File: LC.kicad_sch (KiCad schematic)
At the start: 41 parts, among them J4 Conn_01x01_Pin, J5 Conn_01x01_Pin, J6 Conn_01x01_Pin, Q10 NMOS, Q11 NMOS, Q12 NMOS, Q7 NMOS, Q8 NMOS, Q9 NMOS, U3 OPA2196xDGK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

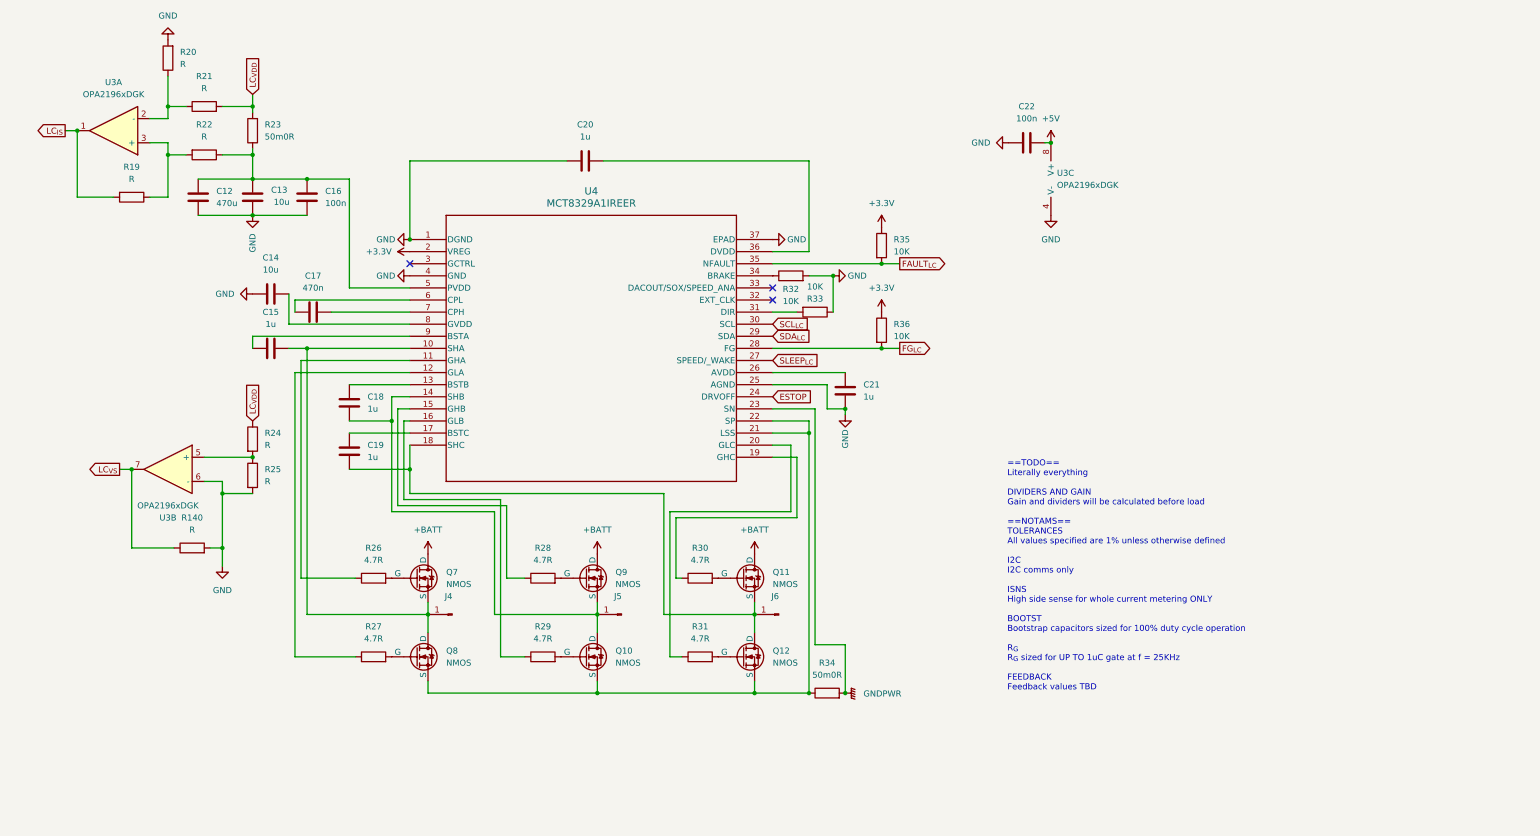
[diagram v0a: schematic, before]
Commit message: The great decluttering
Moved all possible controls to I2C, part selection commenced, IOs assigned pending comms schema
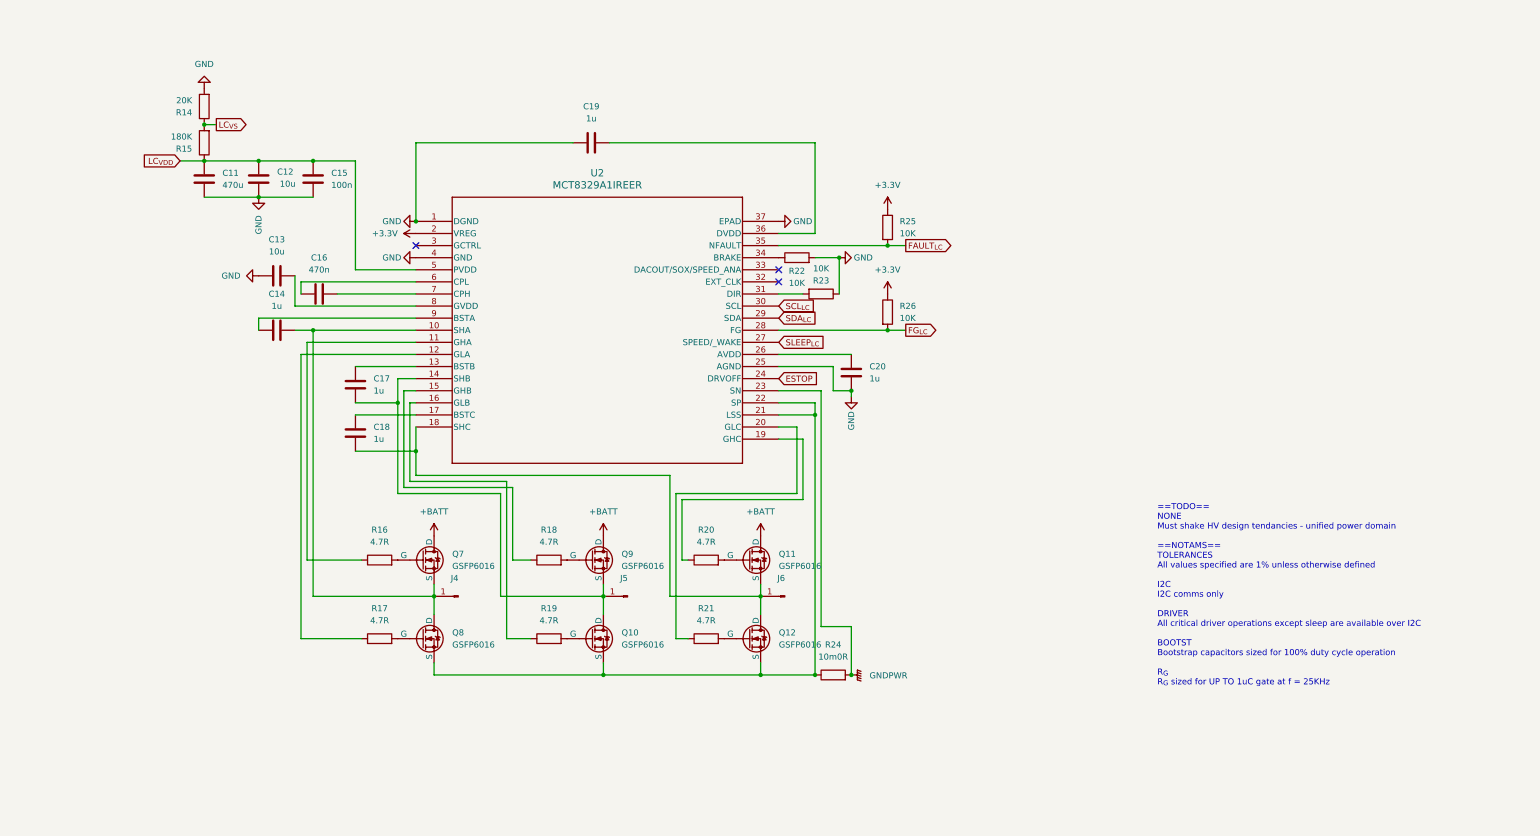
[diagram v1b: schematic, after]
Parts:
- removed C21: 1u, Capacitor_SMD:C_0603_1608Metric, symbol Device:C
- removed C22: 100n, Capacitor_SMD:C_0603_1608Metric, symbol Device:C
- removed R140: R, Resistor_SMD:R_0603_1608Metric_Pad0.98x0.95mm_HandSolder, symbol Device:R
- removed R27, R28, R29, R30, R31: 4.7R, Resistor_SMD:R_1206_3216Metric, symbol Device:R
- removed R32, R33, R35, R36: 10K, Resistor_SMD:R_0603_1608Metric_Pad0.98x0.95mm_HandSolder, symbol Device:R
- removed R34: 50m0R, Resistor_SMD:R_1206_3216Metric, symbol Device:R
- removed U3: OPA2196xDGK, Package_SO:VSSOP-8_3x3mm_P0.65mm, symbol Amplifier_Operational:OPA2196xDGK
- removed U4: MCT8329A1IREER, footprints:WQFN36_REE_TEX, symbol MCT8329:MCT8329A1IREER
- added C11: 470u, Capacitor_SMD:C_0603_1608Metric, symbol Device:C
- added R14: 20K, Resistor_SMD:R_0603_1608Metric_Pad0.98x0.95mm_HandSolder, symbol Device:R
- added R15: 180K, Resistor_SMD:R_0603_1608Metric_Pad0.98x0.95mm_HandSolder, symbol Device:R
- added R16, R17, R18: 4.7R, Resistor_SMD:R_1206_3216Metric, symbol Device:R
- added U2: MCT8329A1IREER, footprints:WQFN36_REE_TEX, symbol MCT8329:MCT8329A1IREER
- C12: value 470u -> 10u
- C14: value 10u -> 1u
- C15: value 1u -> 100n
- C16: value 100n -> 470n
- C17: value 470n -> 1u
- Q10, Q11, Q12, Q7, Q8, Q9: value NMOS -> GSFP6016; footprint (none) -> Package_DFN_QFN:PQFN-8-EP_6x5mm_P1.27mm_Generic
- R19, R20, R21: value R -> 4.7R; footprint Resistor_SMD:R_0603_1608Metric_Pad0.98x0.95mm_HandSolder -> Resistor_SMD:R_1206_3216Metric
- R22, R25: value R -> 10K
- R23: value 50m0R -> 10K; footprint Resistor_SMD:R_1206_3216Metric -> Resistor_SMD:R_0603_1608Metric_Pad0.98x0.95mm_HandSolder
- R24: value R -> 10m0R; footprint Resistor_SMD:R_0603_1608Metric_Pad0.98x0.95mm_HandSolder -> Resistor_SMD:R_1206_3216Metric
- R26: value 4.7R -> 10K; footprint Resistor_SMD:R_1206_3216Metric -> Resistor_SMD:R_0603_1608Metric_Pad0.98x0.95mm_HandSolder
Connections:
- net LC_{IS} is gone; now on an unnamed net: R19.2
- net +3.3V: now also R25.1, R26.1, U2.2 (VREG)
- net ESTOP: now also U2.24 (DRVOFF)
- net FAULT_{LC}: now also R25.2, U2.35 (NFAULT)
- net FG_{LC}: now also R26.2, U2.28 (FG)
- net GND: now also C13.1, C15.2, C19.1, R22.2, R23.1, C11.2, R14.2, U2.1 (DGND), U2.25 (AGND), U2.37 (EPAD), U2.4 (GND); no longer C13.2, C14.1, C16.2, R20.2, R25.2
- net GNDPWR: now also R24.2, U2.23 (SN)
- net LC_{VDD}: now also C12.1, C15.1, C11.1, R15.1, U2.5 (PVDD); no longer R21.2, R23.2, R24.1
- net LC_{VS}: now also R14.1, R15.2
- net SCL_{LC}: now also U2.30 (SCL)
- net SDA_{LC}: now also U2.29 (SDA)
- net SLEEP_{LC}: now also U2.27 (SPEED/_WAKE)
- net at J6.1 (Pin_1), Q11.3 (S), Q12.1 (D): now also C18.2, U2.18 (SHC); no longer C19.2
- net at J5.1 (Pin_1), Q10.1 (D), Q9.3 (S): now also C17.2, U2.14 (SHB); no longer C18.2
- net at Q10.3 (S), Q12.3 (S), Q8.3 (S): now also R24.1, U2.21 (LSS), U2.22 (SP)
- net at R19.1: now also U2.16 (GLB); no longer R22.2
- net at R20.1: now also U2.19 (GHC); no longer R21.1
- net at Q11.2 (G): now also R20.2
- net at Q7.2 (G): now also R16.2; no longer R26.2
- net at J4.1 (Pin_1), Q7.3 (S), Q8.1 (D): now also C14.1, U2.10 (SHA); no longer C15.1
- net at Q9.2 (G): now also R18.2
- net at C18.1: now also U2.17 (BSTC)
- net at C20.2: now also U2.26 (AVDD)
- net at C17.1: now also U2.13 (BSTB)
- net at C14.2: now also U2.9 (BSTA)
- net at Q12.2 (G): now also R21.2
- net at Q8.2 (G): now also R17.2
- new net: C13.2, U2.8 (GVDD)
- new net: R18.1, U2.15 (GHB)
- new net: C19.2, U2.36 (DVDD)
- new net: C16.1, U2.6 (CPL)
- new net: C16.2, U2.7 (CPH)
- new net: R21.1, U2.20 (GLC)
- new net: R23.2, U2.31 (DIR)
- new net: R16.1, U2.11 (GHA)
- new net: R22.1, U2.34 (BRAKE)
- new net: R17.1, U2.12 (GLA)
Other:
- note added: "==TODO== NONE Must shake HV design tendancies - unified power domain ==NOTAMS== TOLERANCES All values specified are 1% unless otherwise defined I2C I2C comms only DRIVER All critical driver operations except sleep are available over I2C BOOTST Bootstrap capacitors sized for 100% duty cycle operation R_{G} R_{G} sized for UP TO 1uC gate at f = 25KHz"
- note removed: "==TODO== Literally everything DIVIDERS AND GAIN Gain and dividers will be calculated before load ==NOTAMS== TOLERANCES All values specified are 1% unless otherwise defined I2C I2C comms only ISNS High side sense for whole current metering ONLY BOOTST Bootstrap capacitors sized for 100% duty cycle operation R_{G} R_{G} sized for UP TO 1uC gate at f = 25KHz FEEDBACK Feedback values TBD"

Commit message: Powerstage
Powerstage layout, non critical changes to schematic
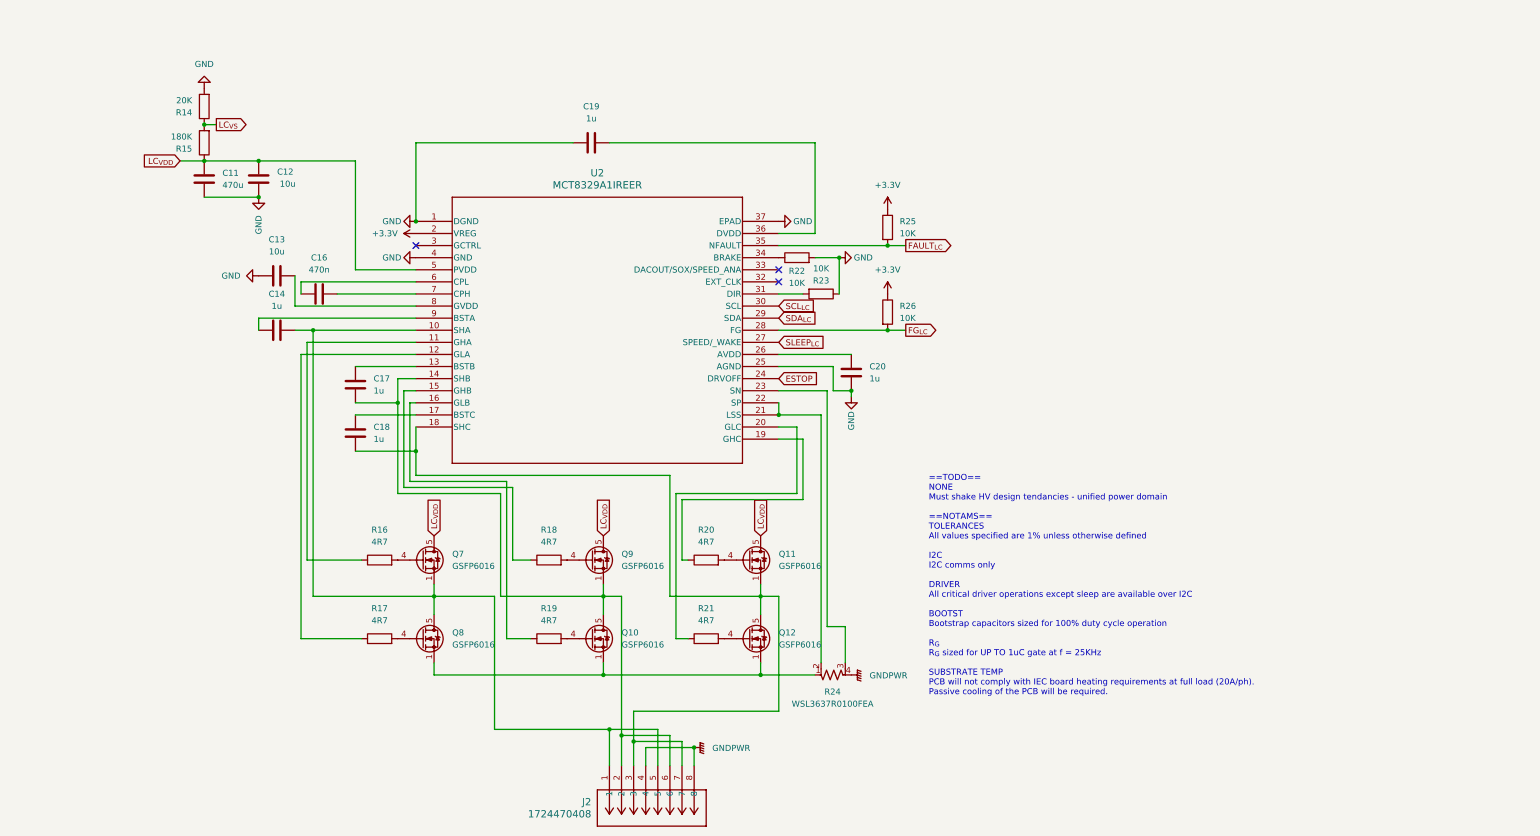
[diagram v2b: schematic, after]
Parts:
- removed C15: 100n, Capacitor_SMD:C_0603_1608Metric, symbol Device:C
- removed J4, J5, J6: Conn_01x01_Pin, symbol Connector:Conn_01x01_Pin
- removed Q10, Q11, Q12, Q7, Q8, Q9: GSFP6016, Package_DFN_QFN:PQFN-8-EP_6x5mm_P1.27mm_Generic, symbol Simulation_SPICE:NMOS
- removed R24: 10m0R, Resistor_SMD:R_1206_3216Metric, symbol Device:R
- added J2: 1724470408, footprints:CONN08_1724470408_MOL, symbol 1724470408:1724470408
- added Q10, Q11, Q12, Q7, Q8, Q9: GSFP6016, Package_SO:PowerPAK_SO-8_Single, symbol Transistor_FET:SiR696DP
- added R24: WSL3637R0100FEA, WSL3637_VIS, symbol WSL3637R0100FEA:WSL3637R0100FEA
- C11: footprint Capacitor_SMD:C_0603_1608Metric -> Capacitor_THT:CP_Radial_D10.0mm_P5.00mm
- C12: footprint Capacitor_SMD:C_0603_1608Metric -> Capacitor_SMD:C_1210_3225Metric
- C13: footprint Capacitor_SMD:C_0603_1608Metric -> Capacitor_SMD:C_0402_1005Metric
- C14, C16, C17, C18, C19, C20: footprint Capacitor_SMD:C_0603_1608Metric -> Capacitor_SMD:C_0201_0603Metric
- R14, R15, R22, R23, R25, R26: footprint Resistor_SMD:R_0603_1608Metric_Pad0.98x0.95mm_HandSolder -> Resistor_SMD:R_0201_0603Metric
- R16, R17, R18, R19, R20, R21: value 4.7R -> 4R7; footprint Resistor_SMD:R_1206_3216Metric -> Resistor_SMD:R_0603_1608Metric
- U2: footprint footprints:WQFN36_REE_TEX -> WQFN36_REE_TEX
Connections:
- net GNDPWR: now also J2.4, J2.8, R24.4; no longer U2.23 (SN)
- net LC_{VDD}: now also Q11.5 (D), Q7.5 (D), Q9.5 (D)
- net at R16.2: now also Q7.4 (G)
- net at C14.1, U2.10 (SHA): now also J2.1, J2.5, Q7.1 (S), Q7.2 (S), Q7.3 (S), Q8.5 (D)
- net at R18.2: now also Q9.4 (G)
- net at R20.2: now also Q11.4 (G)
- net at C18.2, U2.18 (SHC): now also J2.3, J2.7, Q11.1 (S), Q11.2 (S), Q11.3 (S), Q12.5 (D)
- net at C17.2, U2.14 (SHB): now also J2.2, J2.6, Q10.5 (D), Q9.1 (S), Q9.2 (S), Q9.3 (S)
- net at U2.21 (LSS), U2.22 (SP): now also R24.2
- net at R21.2: now also Q12.4 (G)
- net at R19.2: now also Q10.4 (G)
- net at C16.1: now also U2.7 (CPH); no longer U2.6 (CPL)
- net at C16.2: now also U2.6 (CPL); no longer U2.7 (CPH)
- net at R17.2: now also Q8.4 (G)
- new net: Q10.1 (S), Q10.2 (S), Q10.3 (S), Q12.1 (S), Q12.2 (S), Q12.3 (S), Q8.1 (S), Q8.2 (S), Q8.3 (S), R24.1
- new net: R24.3, U2.23 (SN)
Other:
- note added: "==TODO== NONE Must shake HV design tendancies - unified power domain ==NOTAMS== TOLERANCES All values specified are 1% unless otherwise defined I2C I2C comms only DRIVER All critical driver operations except sleep are available over I2C BOOTST Bootstrap capacitors sized for 100% duty cycle operation R_{G} R_{G} sized for UP TO 1uC gate at f = 25KHz SUBSTRATE TEMP PCB will not comply with IEC boar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"
- note removed: "==TODO== NONE Must shake HV design tendancies - unified power domain ==NOTAMS== TOLERANCES All values specified are 1% unless otherwise defined I2C I2C comms only DRIVER All critical driver operations except sleep are available over I2C BOOTST Bootstrap capacitors sized for 100% duty cycle operation R_{G} R_{G} sized for UP TO 1uC gate at f = 25KHz"
